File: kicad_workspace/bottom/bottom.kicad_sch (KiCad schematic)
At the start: 66 parts, among them J1 Battery connector, J2 Battery connector, M1 N20_MOTOR_EXTENDED_SHAFT, M2 N20_MOTOR_EXTENDED_SHAFT, U1 DRV8833PWP, U12 ACS712-5A, U13 ACS712-5A, U17 STM32H7A3RITx, U4 BNO055, Y1 32.768kHz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

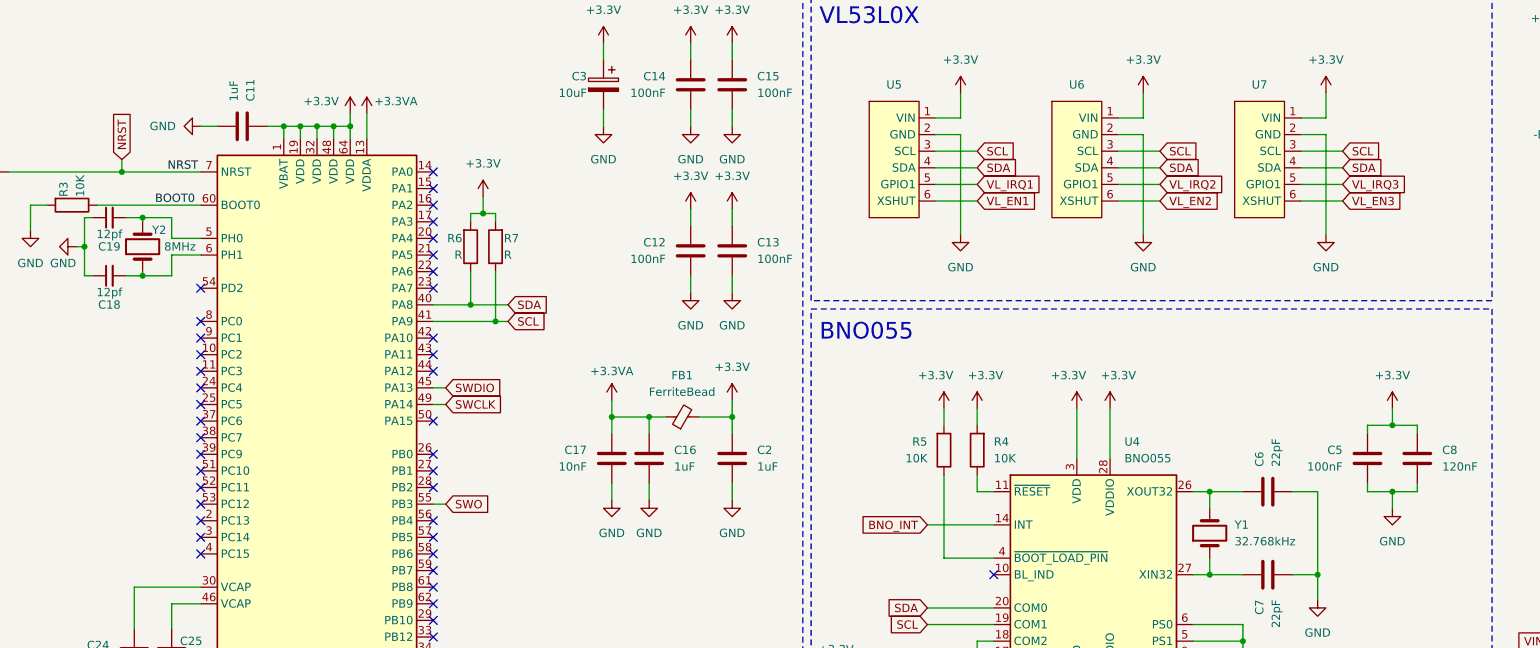
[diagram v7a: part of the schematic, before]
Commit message: wired laser sensors
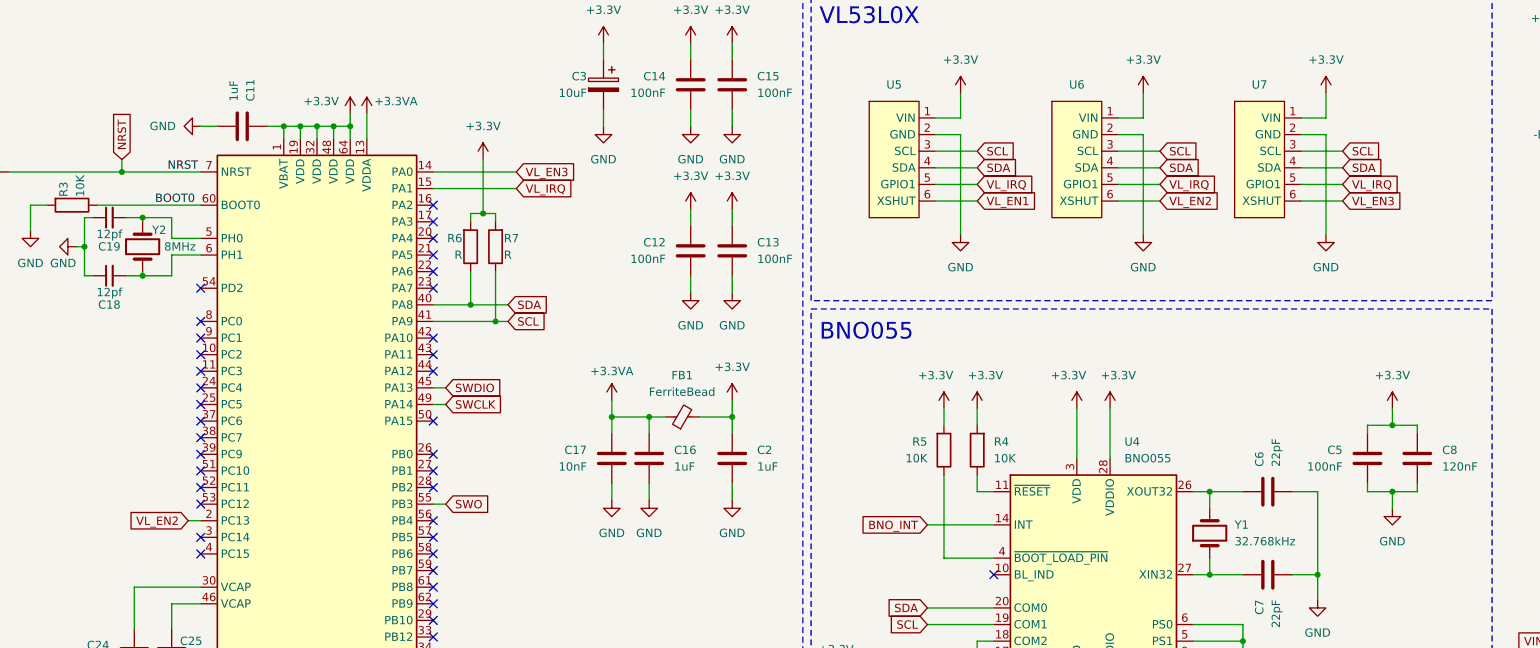
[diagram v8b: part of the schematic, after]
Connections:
- net VL_IRQ1 is gone; now on net VL_IRQ: U5.5 (GPIO1)
- net VL_IRQ2 is gone; now on net VL_IRQ: U6.5 (GPIO1)
- net VL_IRQ3 is gone; now on net VL_IRQ: U7.5 (GPIO1)
- net VL_EN2: now also U17.2 (PC13)
- net VL_EN3: now also U17.14 (PA0)
- net VL_IRQ: now reaches U17.15 (PA1)
- no-connect marks 46 -> 43
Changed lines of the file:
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@@
   (no_connect (at 92.075 59.055))
   (no_connect (at 92.075 66.675))
-  (no_connect (at 92.075 43.815))
   (no_connect (at 92.075 104.775))
   (no_connect (at 92.075 84.455))
@@
   (no_connect (at 56.515 74.295))
   (no_connect (at 56.515 69.215))
-  (no_connect (at 92.075 41.275))
   (no_connect (at 92.075 51.435))
   (no_connect (at 92.075 79.375))
@@
   (no_connect (at 56.515 81.915))
   (no_connect (at 92.075 109.855))
-  (no_connect (at 56.515 94.615))
   (no_connect (at 92.075 112.395))
   (no_connect (at 56.515 76.835))
@@
     (stroke (width 0) (type default))
   )
+  (wire (pts (xy 92.075 41.275) (xy 104.775 41.275))
+    (stroke (width 0) (type default))
+  )
   (wire (pts (xy 196.85 195.58) (xy 196.85 198.12))
     (stroke (width 0) (type default))
@@
     (stroke (width 0) (type default))
   )
-  (wire (pts (xy 99.695 45.085) (xy 99.695 47.625))
+  (wire (pts (xy 99.695 39.37) (xy 99.695 47.625))
     (stroke (width 0) (type default))
   )
@@
     (stroke (width 0) (type default))
   )
+  (wire (pts (xy 92.075 43.815) (xy 104.775 43.815))
+    (stroke (width 0) (type default))
+  )
   (wire (pts (xy 350.52 78.105) (xy 350.52 95.25))
     (stroke (width 0) (type default))
@@
   )
   (wire (pts (xy 348.615 75.565) (xy 344.17 75.565))
+    (stroke (width 0) (type default))
+  )
+  (wire (pts (xy 54.61 94.615) (xy 56.515 94.615))
     (stroke (width 0) (type default))
   )
@@
     )
   )
+  (global_label "VL_EN2" (shape input) (at 54.61 94.615 180) (fields_autoplaced)
+    (effects (font (size 1.27 1.27)) (justify right))
+    (property "Intersheetrefs" "${INTERSHEET_REFS}" (at 44.8515 94.615 0)
+      (effects (font (size 1.27 1.27)) (justify right) hide)
+    )
+  )
+  (global_label "VL_IRQ" (shape input) (at 231.14 43.18 0) (fields_autoplaced)
+    (effects (font (size 1.27 1.27)) (justify left))
+    (property "Intersheetrefs" "${INTERSHEET_REFS}" (at 240.4148 43.18 0)
+      (effects (font (size 1.27 1.27)) (justify left) hide)
+    )
+  )
+  (global_label "VL_IRQ" (shape input) (at 104.775 43.815 0) (fields_autoplaced)
+    (effects (font (size 1.27 1.27)) (justify left))
+    (property "Intersheetrefs" "${INTERSHEET_REFS}" (at 114.0498 43.815 0)
+      (effects (font (size 1.27 1.27)) (justify left) hide)
+    )
+  )
   (global_label "SCL" (shape input) (at 103.505 64.135 0) (fields_autoplaced)
     (effects (font (size 1.27 1.27)) (justify left))
@@
     )
   )
+  (global_label "VL_IRQ" (shape input) (at 203.2 43.18 0) (fields_autoplaced)
+    (effects (font (size 1.27 1.27)) (justify left))
+    (property "Intersheetrefs" "${INTERSHEET_REFS}" (at 212.4748 43.18 0)
+      (effects (font (size 1.27 1.27)) (justify left) hide)
+    )
+  )
   (global_label "SCL" (shape input) (at 231.14 38.1 0) (fields_autoplaced)
     (effects (font (size 1.27 1.27)) (justify left))
@@
     )
   )
+  (global_label "VL_IRQ" (shape input) (at 175.26 43.18 0) (fields_autoplaced)
+    (effects (font (size 1.27 1.27)) (justify left))
+    (property "Intersheetrefs" "${INTERSHEET_REFS}" (at 184.5348 43.18 0)
+      (effects (font (size 1.27 1.27)) (justify left) hide)
+    )
+  )
   (global_label "VL_EN2" (shape input) (at 203.2 45.72 0) (fields_autoplaced)
     (effects (font (size 1.27 1.27)) (justify left))
@@
     )
   )
-  (global_label "VL_IRQ2" (shape input) (at 203.2 43.18 0) (fields_autoplaced)
-    (effects (font (size 1.27 1.27)) (justify left))
-    (property "Intersheetrefs" "${INTERSHEET_REFS}" (at 213.6843 43.18 0)
-      (effects (font (size 1.27 1.27)) (justify left) hide)
-    )
-  )
   (global_label "SCL" (shape input) (at 203.2 38.1 0) (fields_autoplaced)
     (effects (font (size 1.27 1.27)) (justify left))
@@
     )
   )
-  (global_label "VL_IRQ3" (shape input) (at 231.14 43.18 0) (fields_autoplaced)
-    (effects (font (size 1.27 1.27)) (justify left))
-    (property "Intersheetrefs" "${INTERSHEET_REFS}" (at 241.6243 43.18 0)
-      (effects (font (size 1.27 1.27)) (justify left) hide)
-    )
-  )
-  (global_label "VL_IRQ1" (shape input) (at 175.26 43.18 0) (fields_autoplaced)
-    (effects (font (size 1.27 1.27)) (justify left))
-    (property "Intersheetrefs" "${INTERSHEET_REFS}" (at 185.7443 43.18 0)
+  (global_label "VL_EN3" (shape input) (at 104.775 41.275 0) (fields_autoplaced)
+    (effects (font (size 1.27 1.27)) (justify left))
+    (property "Intersheetrefs" "${INTERSHEET_REFS}" (at 114.5335 41.275 0)
       (effects (font (size 1.27 1.27)) (justify left) hide)
     )
@@
     )
   )
-  (symbol (lib_id "power:+3.3V") (at 99.695 45.085 0) (unit 1)
+  (symbol (lib_id "power:+3.3V") (at 99.695 39.37 0) (unit 1)
     (in_bom yes) (on_board yes) (dnp no) (fields_autoplaced)
-    (property "Reference" "#PWR010" (at 99.695 48.895 0)
-      (effects (font (size 1.27 1.27)) hide)
-    )
-    (property "Value" "+3.3V" (at 99.695 40.005 0)
+    (property "Reference" "#PWR010" (at 99.695 43.18 0)
+      (effects (font (size 1.27 1.27)) hide)
+    )
+    (property "Value" "+3.3V" (at 99.695 34.29 0)
       (effects (font (size 1.27 1.27)))
     )
-    (property "Footprint" "" (at 99.695 45.085 0)
-      (effects (font (size 1.27 1.27)) hide)
-    )
-    (property "Datasheet" "" (at 99.695 45.085 0)
-      (effects (font (size 1.27 1.27)) hide)
-    )
+    (property "Footprint" "" (at 99.695 39.37 0)
+      (effects (font (size 1.27 1.27)) hide)
+    )
+    (property "Datasheet" "" (at 99.695 39.37 0)
+      (effects (font (size 1.27 1.27)) hide)
+    )
